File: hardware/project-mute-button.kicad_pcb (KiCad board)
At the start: 2 copper layers, 72.8 x 35.4 mm, 16 parts, among them J1 Conn_01x06_Female, J2 Conn_01x06_Female, J3 Button, J4 Toggle Switch, Q1 Q_NMOS_GSD

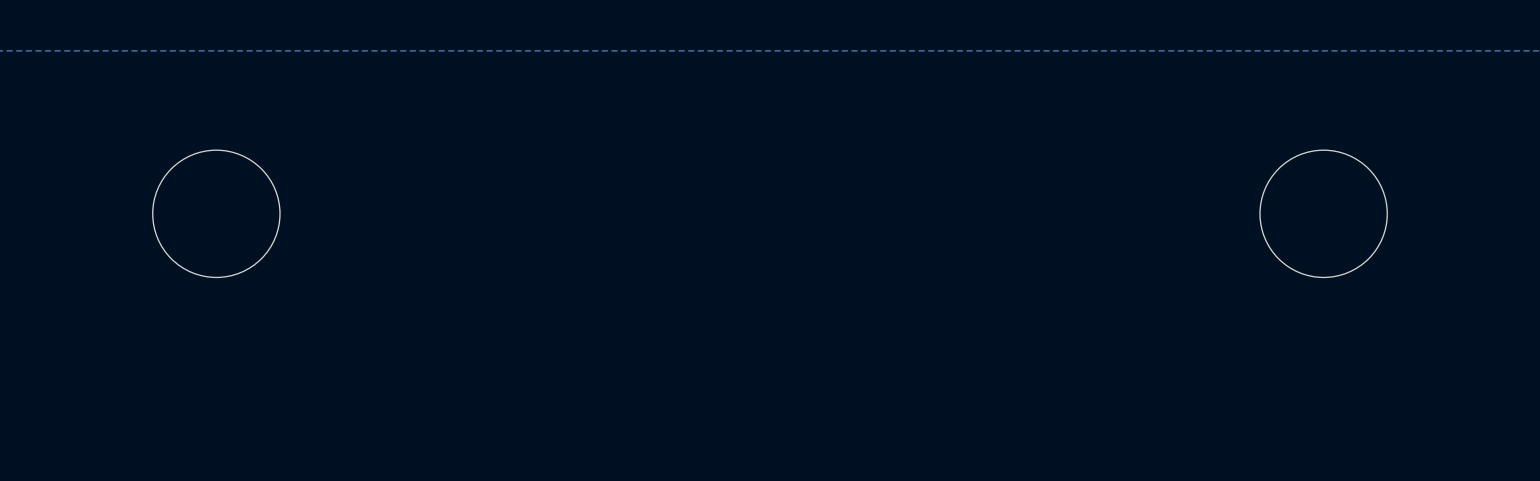
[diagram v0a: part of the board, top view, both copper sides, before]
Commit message: Remove the two mounting holes outside of board
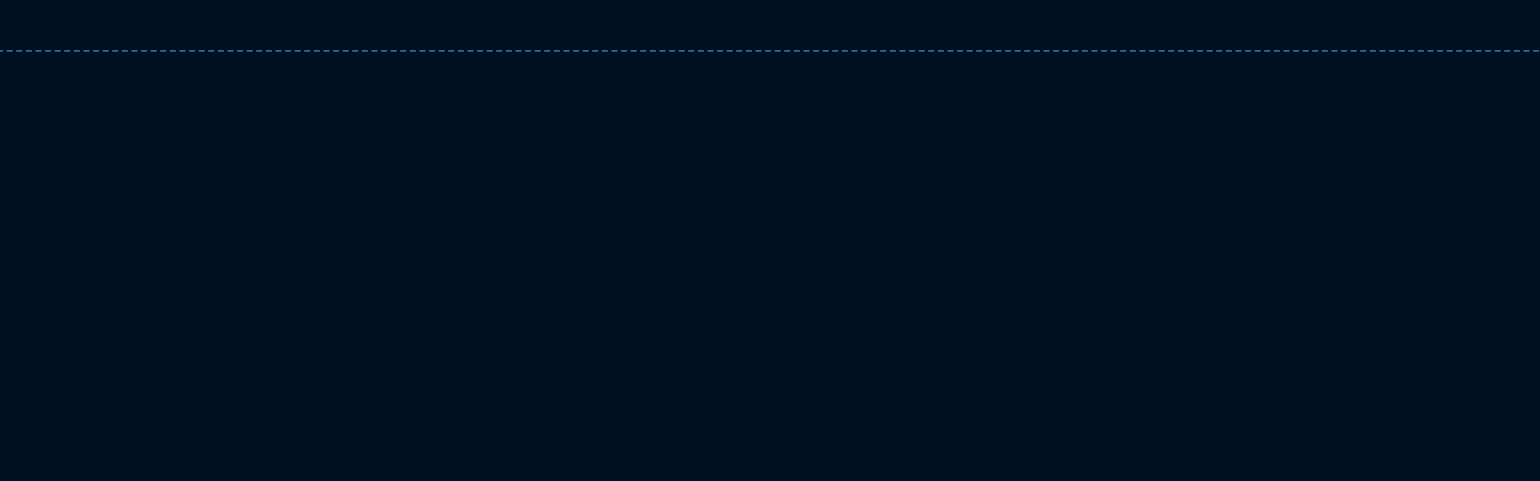
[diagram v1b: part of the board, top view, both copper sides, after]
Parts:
- removed H1, H3: MountingHole, MountingHole:MountingHole_5mm
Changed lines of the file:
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@@
   (general
     (thickness 1.6)
-    (drawings 35)
+    (drawings 37)
     (tracks 65)
     (zones 0)
-    (modules 16)
+    (modules 14)
     (nets 16)
   )
@@
   )
   (module MountingHole:MountingHole_5mm (layer F.Cu)
-    (at 89.1 31.15)
-    (descr "Mounting Hole 5mm, no annular")
-    (tags "mounting hole 5mm no annular")
-    (attr virtual)
-    (fp_text reference H3 (at 0 -6) (layer F.Fab)
-      (effects (font (size 1 1) (thickness 0.15)))
-    )
-    (fp_text value MountingHole (at 0 6) (layer F.Fab)
-      (effects (font (size 1 1) (thickness 0.15)))
-    )
-    (fp_circle (center 0 0) (end 5.25 0) (layer F.CrtYd) (width 0.05))
-    (fp_circle (center 0 0) (end 5 0) (layer Cmts.User) (width 0.15))
-    (fp_text user %R (at 0.3 0) (layer F.Fab)
-      (effects (font (size 1 1) (thickness 0.15)))
-    )
-    (pad 1 np_thru_hole circle (at 0 0) (size 5 5) (drill 5) (layers *.Cu *.Mask))
-  )
-  (module MountingHole:MountingHole_5mm (layer F.Cu)
     (at 45.6 89.15)
     (descr "Mounting Hole 5mm, no annular")
@@
     (attr virtual)
     (fp_text reference H2 (at 0 -6) (layer F.Fab)
-      (effects (font (size 1 1) (thickness 0.15)))
-    )
-    (fp_text value MountingHole (at 0 6) (layer F.Fab)
-      (effects (font (size 1 1) (thickness 0.15)))
-    )
-    (fp_circle (center 0 0) (end 5.25 0) (layer F.CrtYd) (width 0.05))
-    (fp_circle (center 0 0) (end 5 0) (layer Cmts.User) (width 0.15))
-    (fp_text user %R (at 0.3 0) (layer F.Fab)
-      (effects (font (size 1 1) (thickness 0.15)))
-    )
-    (pad 1 np_thru_hole circle (at 0 0) (size 5 5) (drill 5) (layers *.Cu *.Mask))
-  )
-  (module MountingHole:MountingHole_5mm (layer F.Cu)
-    (at 45.6 31.15)
-    (descr "Mounting Hole 5mm, no annular")
-    (tags "mounting hole 5mm no annular")
-    (attr virtual)
-    (fp_text reference H1 (at 0 -6) (layer F.Fab)
       (effects (font (size 1 1) (thickness 0.15)))
     )
@@
     )
   )
+  (gr_circle (center 89.1 31.15) (end 91.6 31.15) (layer Dwgs.User) (width 0.15))
+  (gr_circle (center 45.6 31.15) (end 48.1 31.15) (layer Dwgs.User) (width 0.15))
   (gr_text "François Gervais\n6 novembre 2022\nv1.0.0" (at 78.65 78.75) (layer F.SilkS)
     (effects (font (size 1 1) (thickness 0.15)) (justify left))
